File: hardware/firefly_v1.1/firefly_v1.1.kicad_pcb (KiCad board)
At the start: 2 copper layers, 31.2 x 10.2 mm, 9 parts, among them J1 Conn_01x02, J2 Conn_01x04, Q1 IRLML6344, U1 MSP430G2231IN14

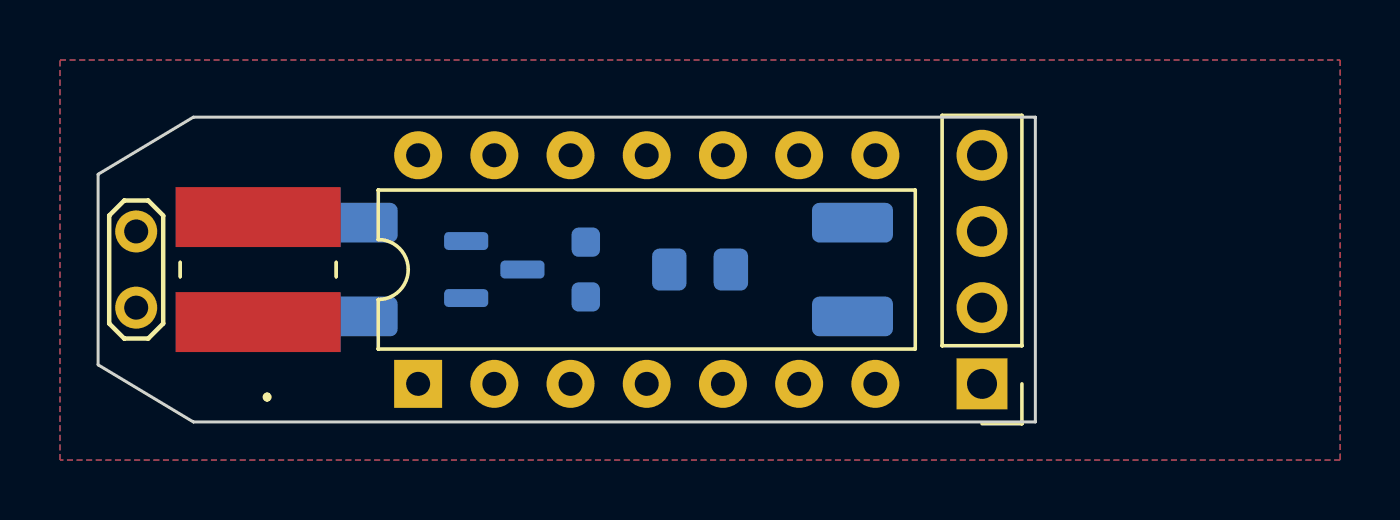
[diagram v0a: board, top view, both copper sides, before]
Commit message: Completed routing
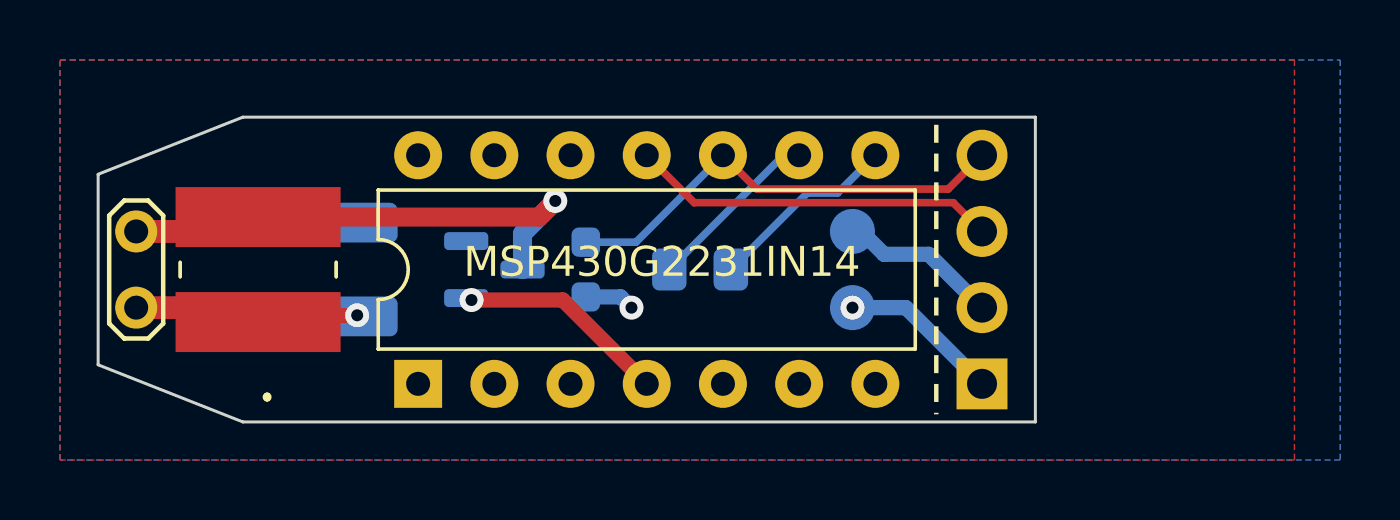
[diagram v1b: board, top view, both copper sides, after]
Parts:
- added J3: GND, TestPoint:TestPoint_Pad_D1.5mm, B.Cu at (159.5, 93.5)
- J1: value Conn_01x02 -> VCC; footprint Capacitor_SMD:C_1210_3225Metric_Pad1.33x2.70mm_HandSolder -> TestPoint:TestPoint_Pad_D1.5mm
- moved J1 1.27 mm to (159.5, 96.0), turned to 0 degrees
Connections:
- C1 pad 1: Net-(D2-K) -> /Vcc
- D2 pad 1: Net-(D2-K) -> /Vcc
- J1 pad 1: GND -> /Vcc
- J2 pad 1: Net-(D2-K) -> /Vcc
- L1 pad 1: Net-(D2-K) -> /Vcc
- R1 pad 1: Net-(D2-K) -> /Vcc
- U1 pad 1: Net-(D2-K) -> /Vcc
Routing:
- net Net-(D2-A): track 0.00 -> 17.6 mm, vias 0 -> 1
- net Net-(J2-Pin_4): track 0.00 -> 15.3 mm
- net /Vcc: track 0.00 -> 15.0 mm, vias 0 -> 3
- net Net-(J2-Pin_3): track 0.00 -> 12.2 mm
- net Net-(Q1-G): track 0.00 -> 7.00 mm, vias 0 -> 1
- net Net-(D1-A): track 0.00 -> 6.40 mm
- net Net-(D1-K): track 0.00 -> 5.91 mm
- net GND: track 0.00 -> 5.49 mm
- added copper zone on F.Cu, net /Vcc
- added copper zone on B.Cu, net GND
- removed copper zone on B.Cu, net (none)
- removed copper zone on F.Cu, net (none)
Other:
- outline, holes or cut-outs redrawn
- board text added: "v1.1"
- board text removed: "v1.0"
